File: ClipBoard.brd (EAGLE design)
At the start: 32.7 x 20.3 mm, 11 parts, among them Q1 IRF520, Q2 IRF520, SW1 DPDT

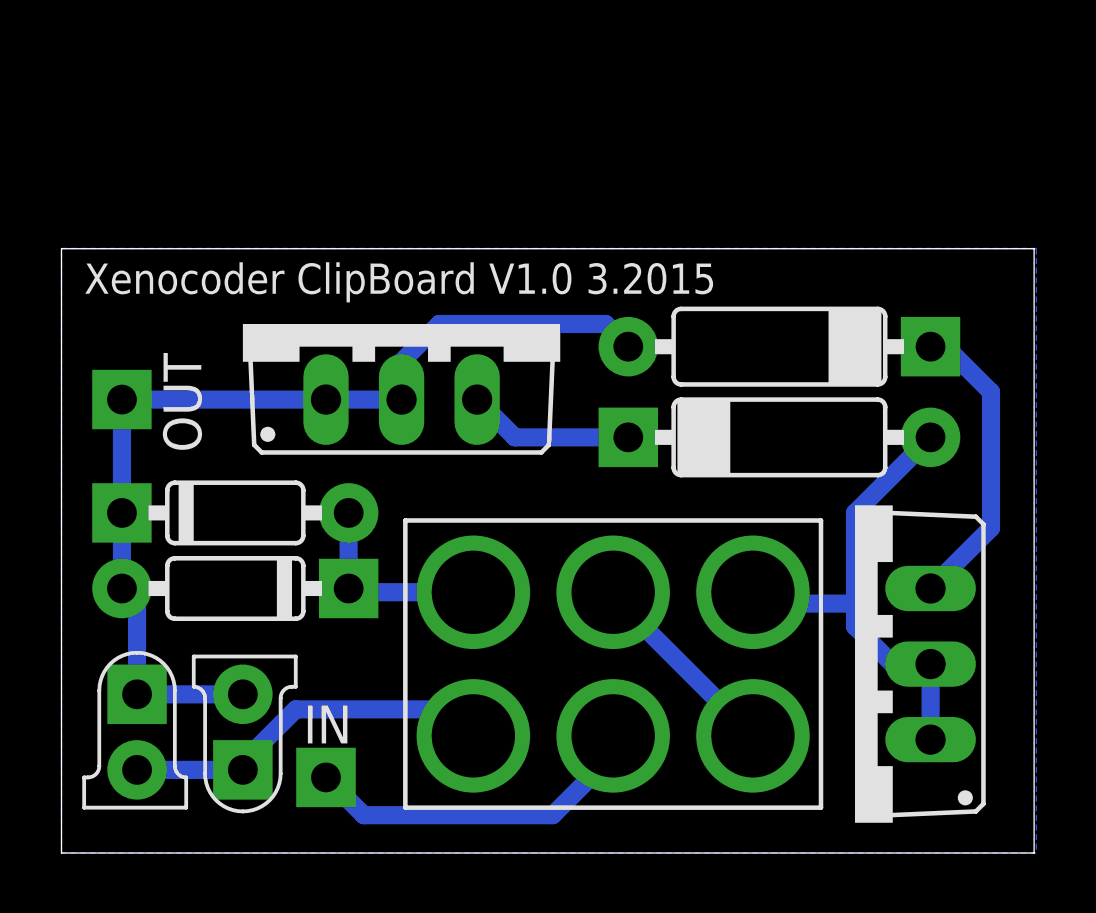
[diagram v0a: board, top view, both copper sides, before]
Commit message: Changes to board and schematic to make v1.1
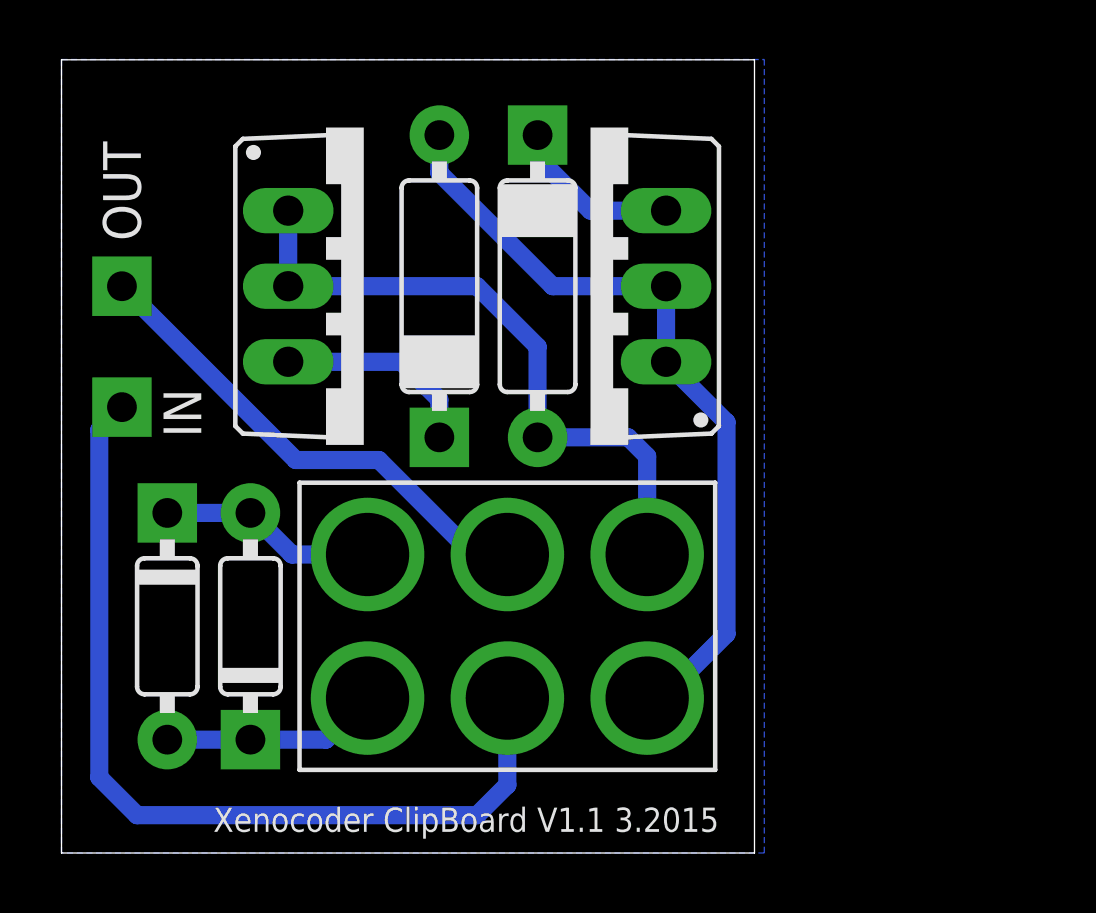
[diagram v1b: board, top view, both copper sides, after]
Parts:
- removed D1, D2: 3MM, mb_diodes:LED3MM
- moved Q1 15.5 mm to (17.8, 19.1)
- moved IN 14.2 mm to (2.03, 15.0)
- moved D6 12.5 mm to (12.7, 19.1), turned to 90 degrees
- moved D5 8.38 mm to (16.0, 19.1), turned to 270 degrees
- moved D3 4.44 mm to (3.56, 7.62), turned to 270 degrees
- moved OUT 3.81 mm to (2.03, 19.1)
- moved SW1 3.78 mm to (15.0, 7.62)
- moved Q2 1.80 mm to (10.2, 19.1), turned to 270 degrees
- moved D4 1.37 mm to (6.35, 7.62), turned to 90 degrees
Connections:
- removed net N$9: SW1.A3, SW1.B1
- new net N$3: OUT.1, SW1.B1
- net N$1: now also D3.C, D4.A, SW1.B2; no longer D1.A, D2.K, SW1.A2
- net N$5: now also SW1.A3; no longer SW1.B3
- net N$7: now also SW1.A2; no longer SW1.B2
- net N$8: now also SW1.B3; no longer D1.K, D2.A, D3.C, D4.A, OUT.1
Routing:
- net N$6: track 11.7 -> 30.3 mm
- net N$3: track 0.00 -> 16.7 mm
- net N$8: track 32.8 -> 22.1 mm
- net N$5: track 16.6 -> 26.6 mm
- net N$9: track 6.77 -> 0.00 mm
- net N$1: track 12.9 -> 7.31 mm
- net N$2: track 10.1 -> 5.82 mm
- net N$4: track 5.61 -> 6.88 mm
- net N$7: track 6.78 -> 7.31 mm
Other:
- board size 32.7 x 20.3 mm -> 23.3 x 26.7 mm
- board text added: "Xenocoder ClipBoard V1.1 3.2015"
- board text removed: "Xenocoder ClipBoard V1.0 3.2015"
